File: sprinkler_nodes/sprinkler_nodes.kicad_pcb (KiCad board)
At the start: 2 copper layers, 94 x 54.6 mm, 67 parts, among them J1 term_block_4-pin, J2 term_block_4-pin, J3 HEADER_1X6, Q1 NPN, Q2 NPN, U1 PIC16F1829_SOIC, U2 Temp_SOT23-3, U3 MP2456, U4 TLV1117_3.3V, U5 NC7SZ125, U6 MPX5100

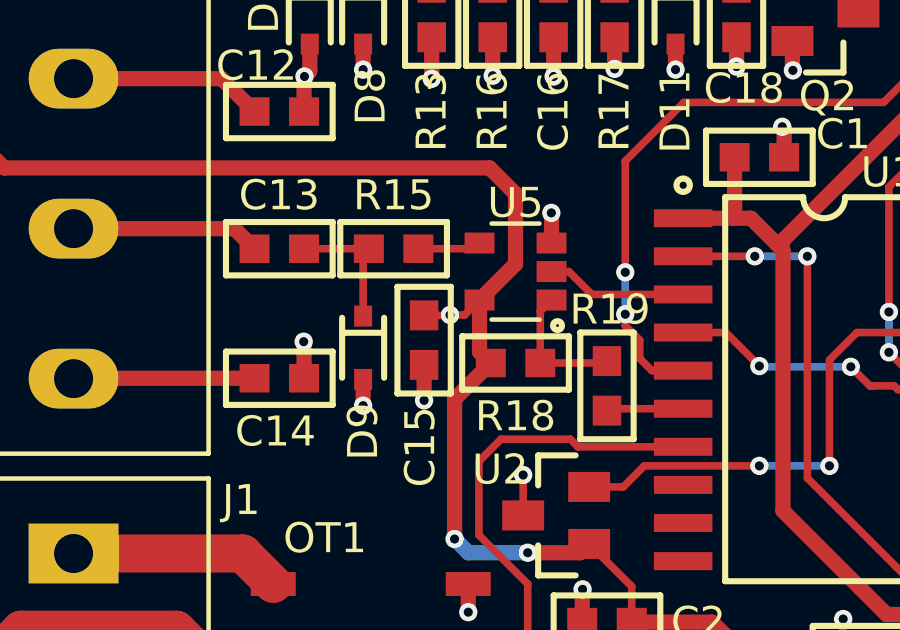
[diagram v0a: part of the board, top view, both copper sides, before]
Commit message: Version 1.0 of sprinkler nodes done.  Functioning except for valve switch.
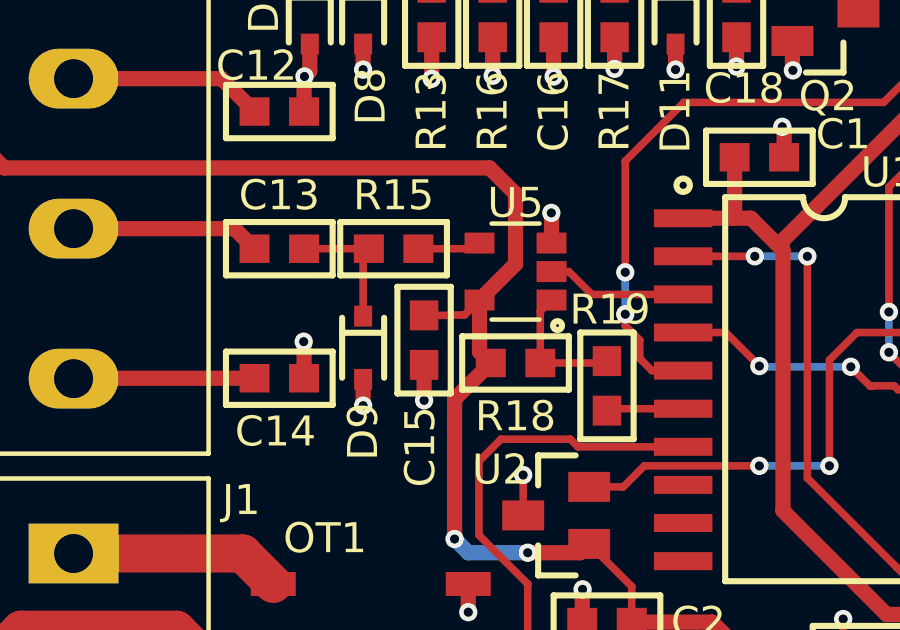
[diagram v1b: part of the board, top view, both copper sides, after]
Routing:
- net +5V: vias 3 -> 2
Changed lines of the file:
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@@
     (thickness 1.6)
     (drawings 17)
-    (tracks 414)
+    (tracks 413)
     (zones 0)
     (modules 67)
@@
   (layers
     (0 F.Cu signal)
-    (31 B.Cu signal hide)
+    (31 B.Cu signal)
     (32 B.Adhes user)
     (33 F.Adhes user)
@@
     (visible_elements FFFDFF7F)
     (pcbplotparams
-      (layerselection 0x010fc_ffffffff)
-      (usegerberextensions false)
+      (layerselection 0x010f0_ffffffff)
+      (usegerberextensions true)
       (usegerberattributes false)
       (usegerberadvancedattributes false)
@@
       (psa4output false)
       (plotreference true)
-      (plotvalue true)
+      (plotvalue false)
       (plotinvisibletext false)
       (padsonsilk false)
@@
       (outputformat 1)
       (mirror false)
-      (drillshape 1)
+      (drillshape 0)
       (scaleselection 1)
-      (outputdirectory ""))
+      (outputdirectory "gerbers/"))
   )
   (net 0 "")
@@
   (segment (start 95.211 63.249) (end 93.69 64.77) (width 0.508) (layer F.Cu) (net 6) (status 800000))
   (segment (start 79.502 47.943) (end 80.3524 47.943) (width 0.254) (layer F.Cu) (net 6) (status 400000))
-  (via (at 80.3656 47.9298) (size 0.6096) (drill 0.3048) (layers F.Cu B.Cu) (net 6))
   (segment (start 80.3524 47.943) (end 80.3656 47.9298) (width 0.254) (layer F.Cu) (net 6))
   (segment (start 80.3656 47.9298) (end 80.8522 47.9298) (width 0.254) (layer F.Cu) (net 6))

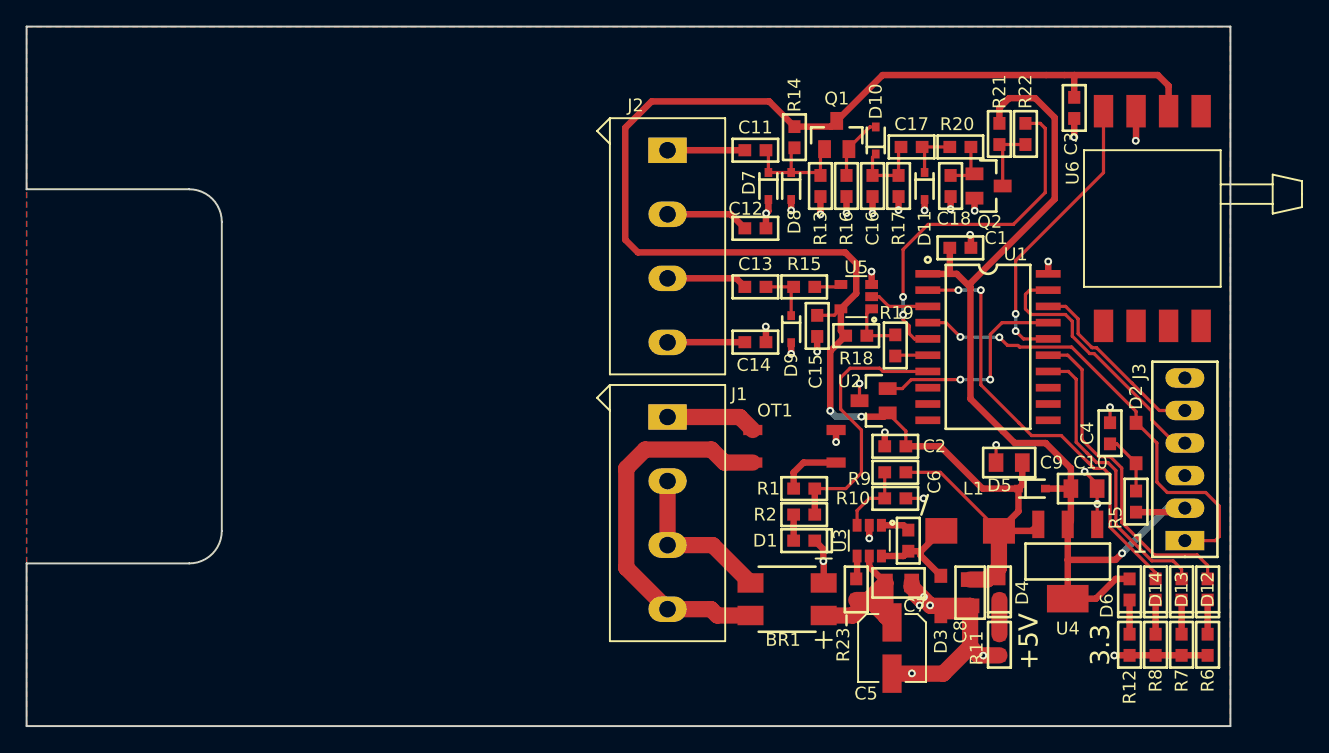
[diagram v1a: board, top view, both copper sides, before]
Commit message: Rev 1.1 Sprinkler Nodes. Added more options for turning on valves
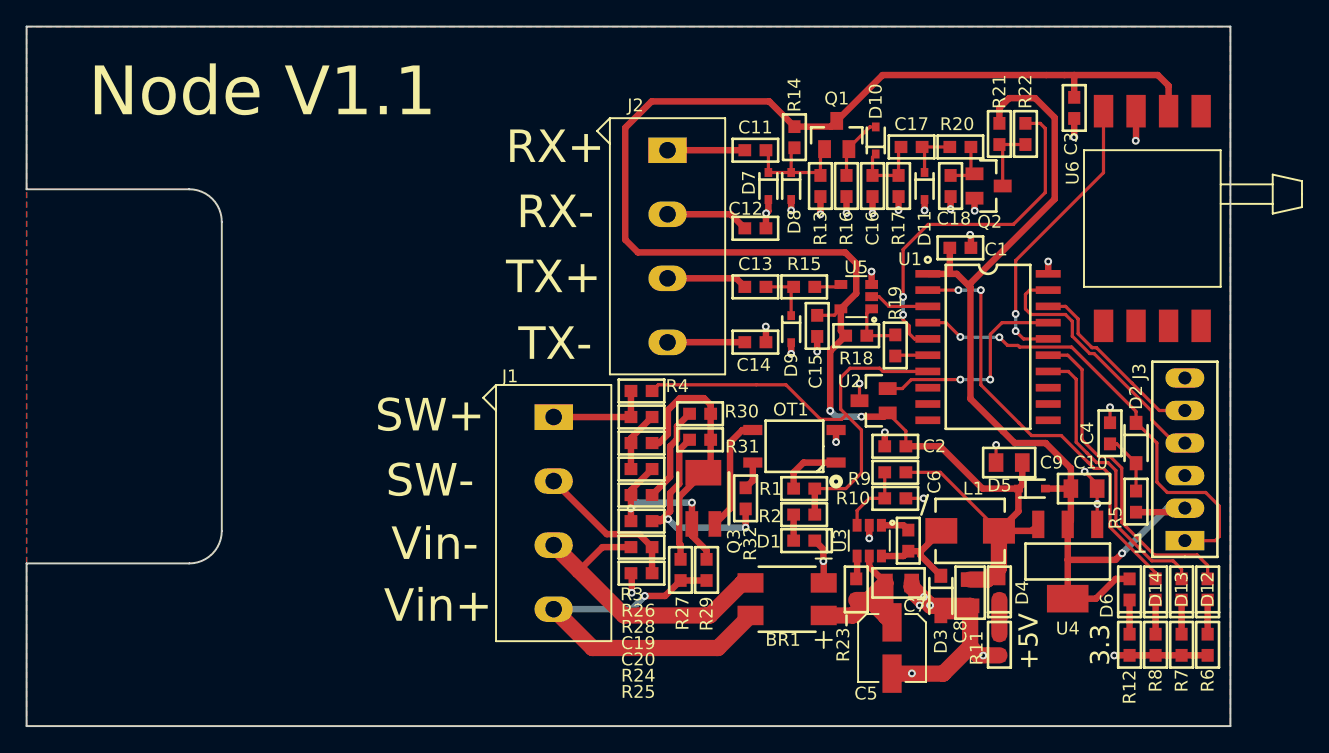
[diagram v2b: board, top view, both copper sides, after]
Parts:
- added C19: CAP_0603, C0603, F.Cu at (65.8, 62.0)
- added C20: CAP_0603, C0603, F.Cu at (65.8, 64.0)
- added Q3: Triac, ICs:Triode SMB-3, F.Cu at (70.6, 62.2)
- added R24: RES_0603, passives:R0603, F.Cu at (65.8, 66.0)
- added R25: RES_0603, passives:R0603, F.Cu at (65.8, 68.1)
- added R26: RES_0603, passives:R0603, F.Cu at (65.8, 57.9)
- added R27: RES_0603, passives:R0603, F.Cu at (68.8, 67.8)
- added R28: RES_0603, passives:R0603, F.Cu at (65.8, 59.9)
- added R29: RES_0603, passives:R0603, F.Cu at (70.9, 67.8)
- added R3: RES_0603, passives:R0603, F.Cu at (65.8, 55.9)
- added R30: RES_0603, passives:R0603, F.Cu at (70.4, 55.6)
- added R31: RES_0603, passives:R0603, F.Cu at (70.4, 57.7)
- added R32: RES_0603, passives:R0603, F.Cu at (73.9, 62.2)
- added R4: RES_0603, passives:R0603, F.Cu at (65.8, 53.8)
- moved J1 8.89 mm to (58.9, 55.9)
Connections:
- J1 pad 1: /SW_24V_1 -> Net-(J1-Pad1)
- J1 pad 2: /VIN_GND -> Net-(J1-Pad2)
- OT1 pad 3: /SW_24V_1 -> /TRIAC_G
- OT1 pad 4: /VIN_AC -> Net-(OT1-Pad4)
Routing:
- net Net-(Q3-Pad2): track 0.00 -> 20.5 mm
- net Net-(C20-Pad1): track 0.00 -> 17.0 mm, vias 0 -> 2
- net /SW_1: track 21.5 -> 38.1 mm
- net Net-(C19-Pad2): track 0.00 -> 14.6 mm, vias 0 -> 2
- net Net-(J1-Pad2): track 0.00 -> 11.9 mm
- net /VIN_GND: track 12.7 -> 23.5 mm
- net /TRIAC_G: track 0.00 -> 9.04 mm
- net Net-(J1-Pad1): track 0.00 -> 8.07 mm
- net Net-(C19-Pad1): track 0.00 -> 7.56 mm
- net /SW_24V_1: track 7.08 -> 0.00 mm
- net /LOAD: track 0.00 -> 4.75 mm
- net Net-(OT1-Pad4): track 0.00 -> 2.20 mm
- net GND: track 73.4 -> 75.0 mm, vias 33 -> 34
- net /VIN_AC: track 29.9 -> 30.5 mm, vias 0 -> 1
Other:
- board text added: "Node V1.1"
- board text added: "RX+"
- board text added: "RX-"
- board text added: "SW+"
- board text added: "SW-"
- board text added: "TX+"
- board text added: "TX-"
- board text added: "Vin+"
- board text added: "Vin-"
